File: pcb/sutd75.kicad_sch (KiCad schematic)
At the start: 44 parts, among them J1 SWD Header, J2 Development header, J3 USB_C_Receptacle_USB2.0, J4 Display I2C, SW1 BOOT0, SW2 BOOT1, SW3 RESET, U1 XC6206PxxxMR, U2 STM32F103RBTx, U3 USBLC6-2SC6

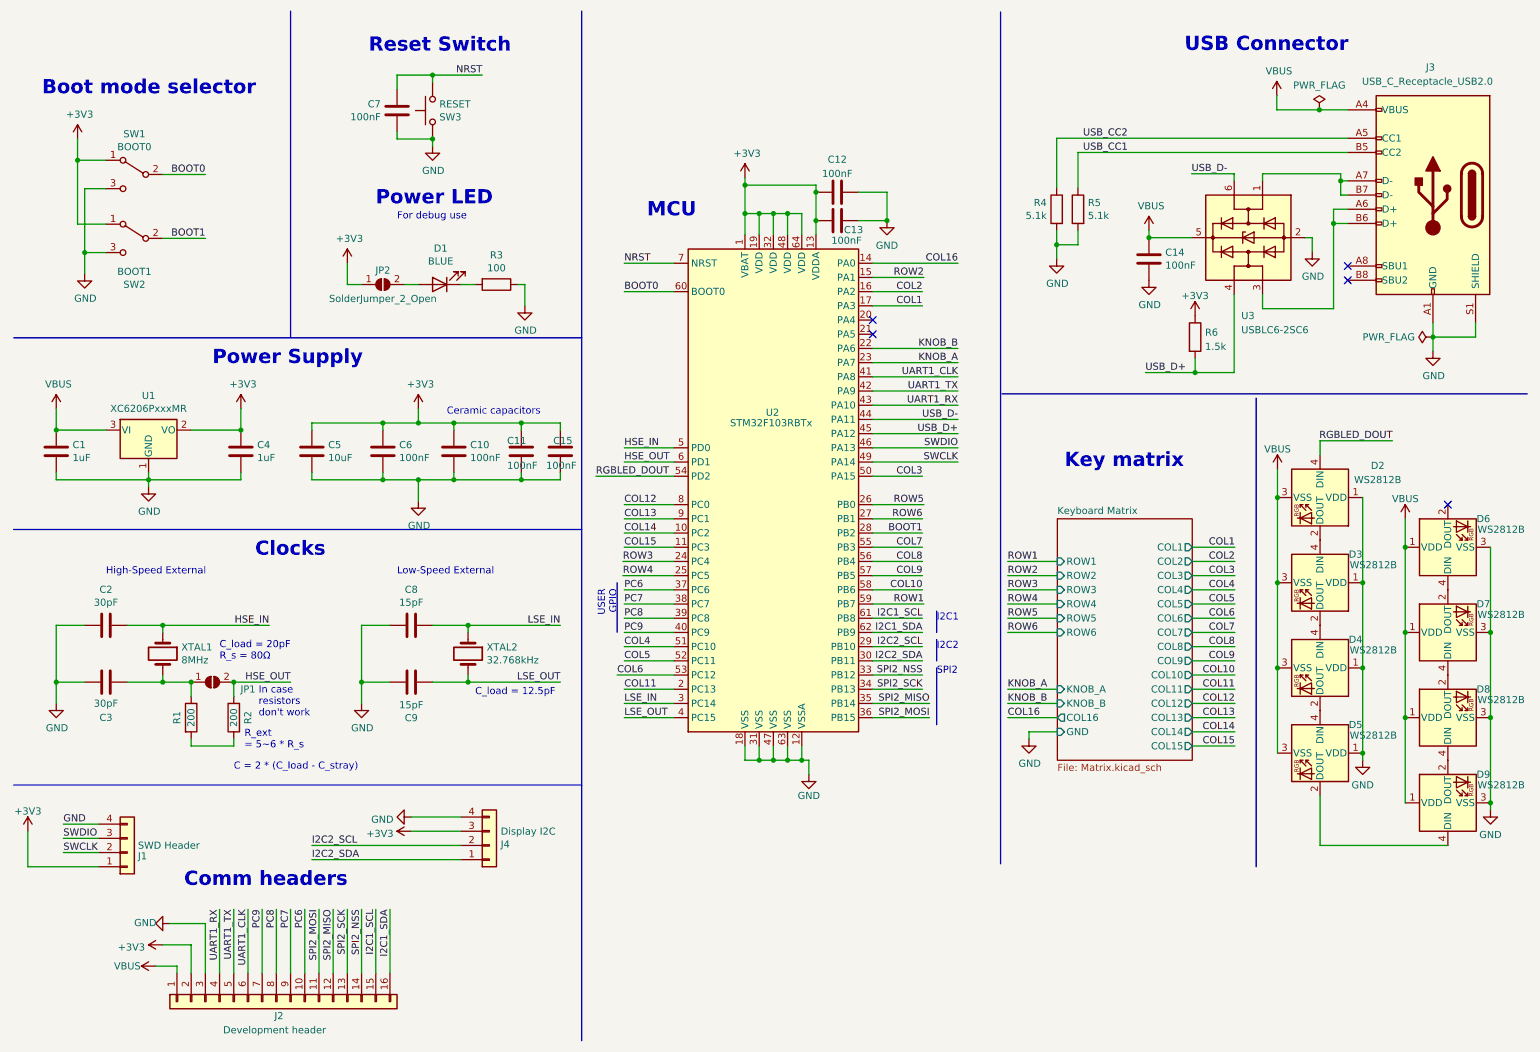
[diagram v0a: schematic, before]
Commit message: Add optional pullup resistors to I2C screen footprint, update footprints
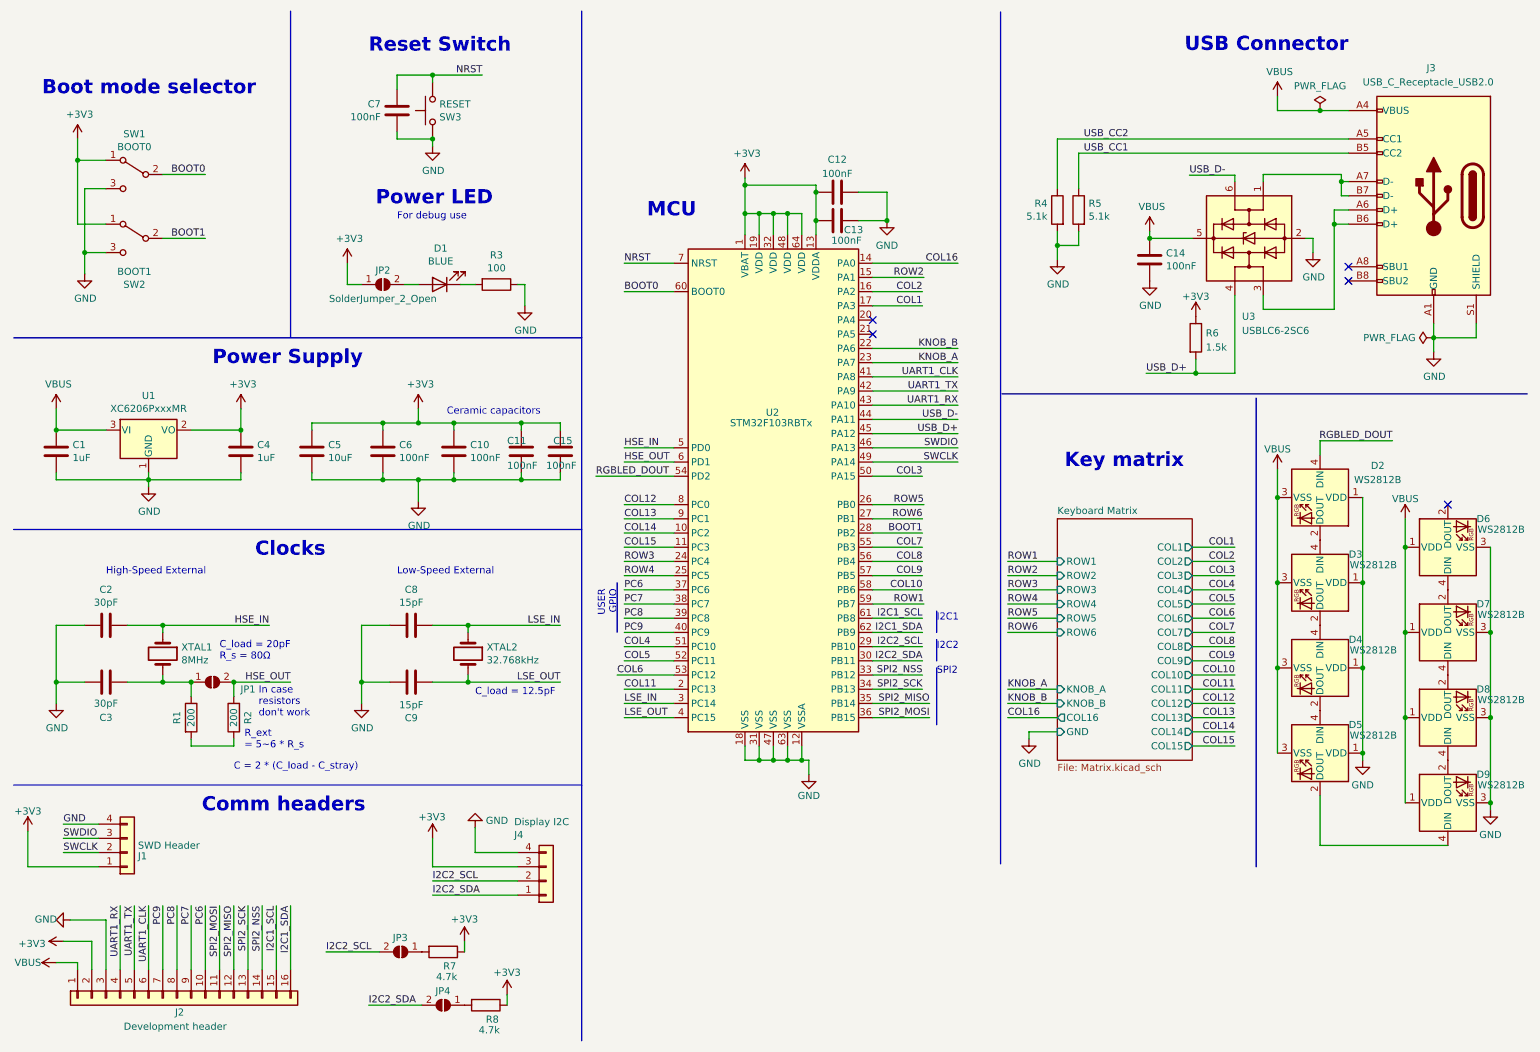
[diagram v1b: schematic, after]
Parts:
- added JP3, JP4: SolderJumper_2_Open, Jumper:SolderJumper-2_P1.3mm_Open_TrianglePad1.0x1.5mm, symbol Jumper:SolderJumper_2_Open
- added R7, R8: 4.7k, Resistor_SMD:R_0402_1005Metric, symbol Device:R
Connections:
- net +3V3: now also R7.1, R8.1
- net I2C2_SCL: now also JP3.2 (B)
- net I2C2_SDA: now also JP4.2 (B)
- new net: JP3.1 (A), R7.2
- new net: JP4.1 (A), R8.2
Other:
- moved on the sheet: J2, J4

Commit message: Touch up silkscreen and schematic
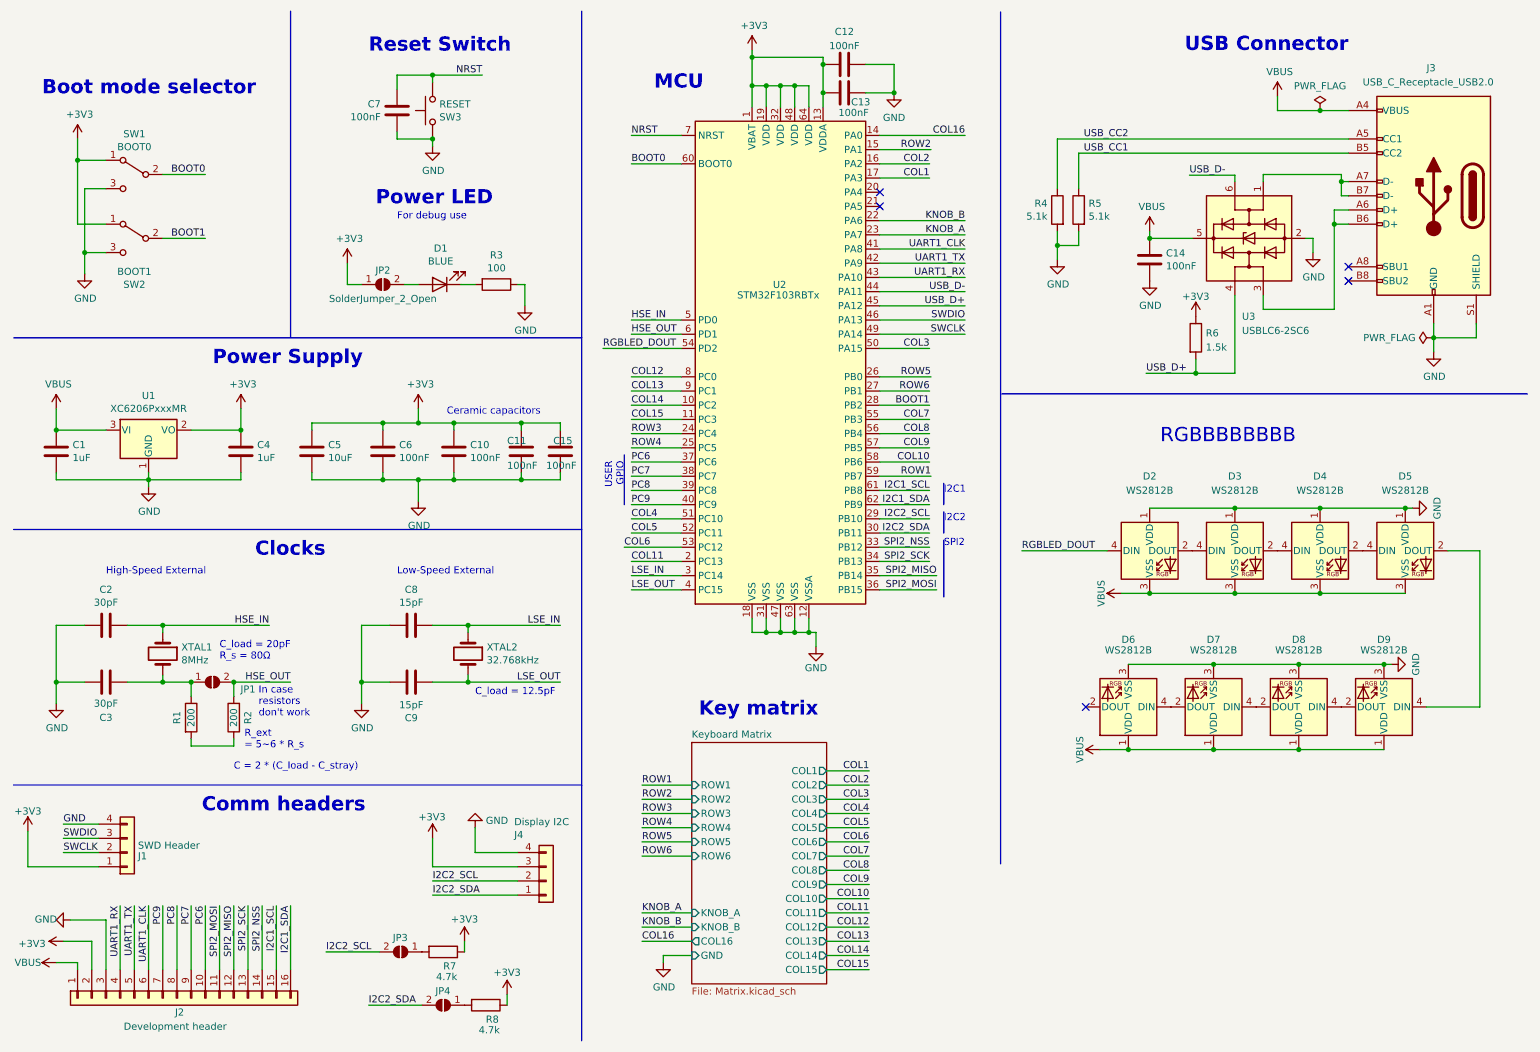
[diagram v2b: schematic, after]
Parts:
- R7, R8: footprint Resistor_SMD:R_0402_1005Metric -> Resistor_SMD:R_0603_1608Metric
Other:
- note added: "RGBBBBBBBB"
- moved on the sheet: C12, C13, D2, D3, D4, D5, D6, D7, D8, D9, U2

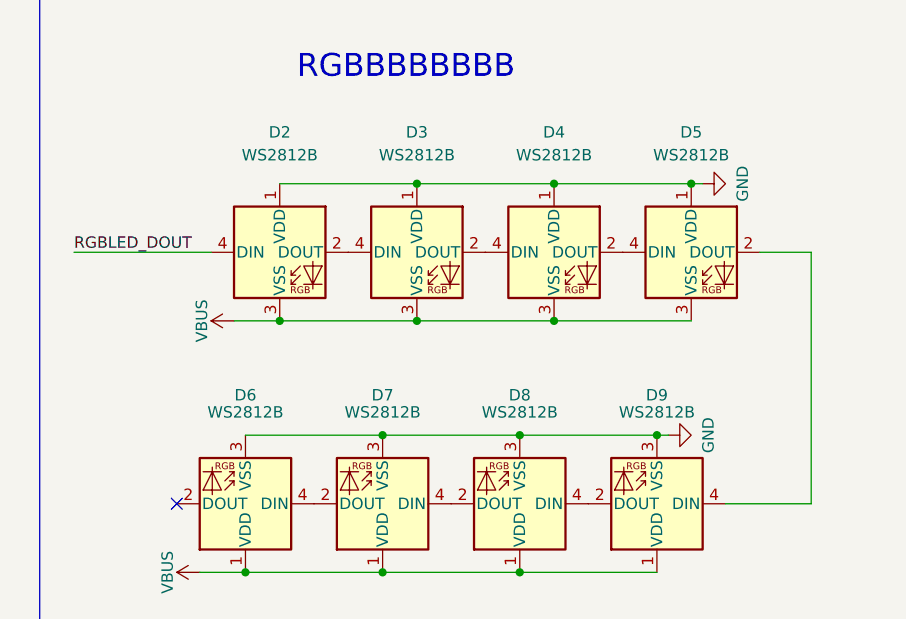
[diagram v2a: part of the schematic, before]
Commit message: Fix SWD silkscreen and boot toggles
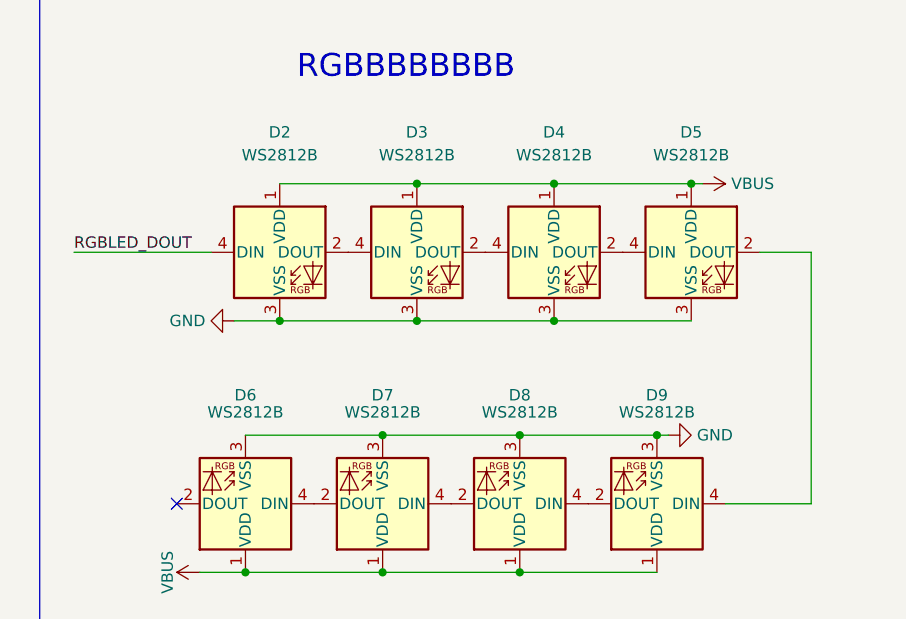
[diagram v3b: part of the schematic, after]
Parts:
- R7, R8: LSCS (none) -> C423031
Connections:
- net GND: now also D2.3 (VSS), D3.3 (VSS), D4.3 (VSS), D5.3 (VSS); no longer D2.1 (VDD), D3.1 (VDD), D4.1 (VDD), D5.1 (VDD)
- net VBUS: now also D2.1 (VDD), D3.1 (VDD), D4.1 (VDD), D5.1 (VDD); no longer D2.3 (VSS), D3.3 (VSS), D4.3 (VSS), D5.3 (VSS)
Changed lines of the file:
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@@
     )
   )
-  (symbol (lib_id "power:GND") (at 264.16 102.235 90) (unit 1)
+  (symbol (lib_id "power:GND") (at 212.09 117.475 270) (unit 1)
     (in_bom yes) (on_board yes) (dnp no) (fields_autoplaced)
-    (property "Reference" "#PWR04" (at 270.51 102.235 0)
-      (effects (font (size 1.27 1.27)) hide)
-    )
-    (property "Value" "GND" (at 268.6034 102.235 0)
-      (effects (font (size 1.27 1.27)))
-    )
-    (property "Footprint" "" (at 264.16 102.235 0)
-      (effects (font (size 1.27 1.27)) hide)
-    )
-    (property "Datasheet" "" (at 264.16 102.235 0)
+    (property "Reference" "#PWR04" (at 205.74 117.475 0)
+      (effects (font (size 1.27 1.27)) hide)
+    )
+    (property "Value" "GND" (at 208.9151 117.475 90)
+      (effects (font (size 1.27 1.27)) (justify right))
+    )
+    (property "Footprint" "" (at 212.09 117.475 0)
+      (effects (font (size 1.27 1.27)) hide)
+    )
+    (property "Datasheet" "" (at 212.09 117.475 0)
       (effects (font (size 1.27 1.27)) hide)
     )
@@
     )
   )
-  (symbol (lib_id "power:VBUS") (at 212.09 117.475 90) (unit 1)
+  (symbol (lib_id "power:VBUS") (at 264.16 102.235 270) (unit 1)
     (in_bom yes) (on_board yes) (dnp no) (fields_autoplaced)
-    (property "Reference" "#PWR03" (at 215.9 117.475 0)
-      (effects (font (size 1.27 1.27)) hide)
-    )
-    (property "Value" "VBUS" (at 208.5142 117.475 0)
-      (effects (font (size 1.27 1.27)))
-    )
-    (property "Footprint" "" (at 212.09 117.475 0)
-      (effects (font (size 1.27 1.27)) hide)
-    )
-    (property "Datasheet" "" (at 212.09 117.475 0)
+    (property "Reference" "#PWR03" (at 260.35 102.235 0)
+      (effects (font (size 1.27 1.27)) hide)
+    )
+    (property "Value" "VBUS" (at 267.335 102.235 90)
+      (effects (font (size 1.27 1.27)) (justify left))
+    )
+    (property "Footprint" "" (at 264.16 102.235 0)
+      (effects (font (size 1.27 1.27)) hide)
+    )
+    (property "Datasheet" "" (at 264.16 102.235 0)
       (effects (font (size 1.27 1.27)) hide)
     )
@@
       (effects (font (size 1.27 1.27)) hide)
     )
-    (property "Value" "GND" (at 264.7934 130.175 0)
-      (effects (font (size 1.27 1.27)))
+    (property "Value" "GND" (at 263.525 130.175 90)
+      (effects (font (size 1.27 1.27)) (justify right))
     )
     (property "Footprint" "" (at 260.35 130.175 0)
@@
       (effects (font (size 1.27 1.27)) hide)
     )
+    (property "LSCS" "C423031" (at 98.425 191.135 90)
+      (effects (font (size 1.27 1.27)) hide)
+    )
     (pin "1")
     (pin "2")
@@
       (effects (font (size 1.27 1.27)) hide)
     )
+    (property "LSCS" "C423031" (at 90.805 181.61 90)
+      (effects (font (size 1.27 1.27)) hide)
+    )

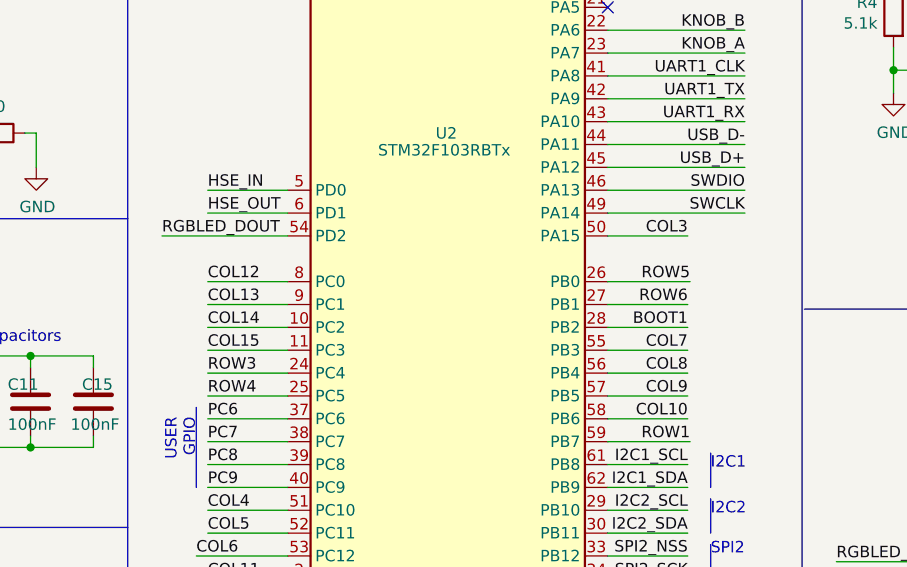
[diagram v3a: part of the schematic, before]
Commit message: Move RGBLED_DIN line to a PWM pin, fix rotary encoder pad overlap
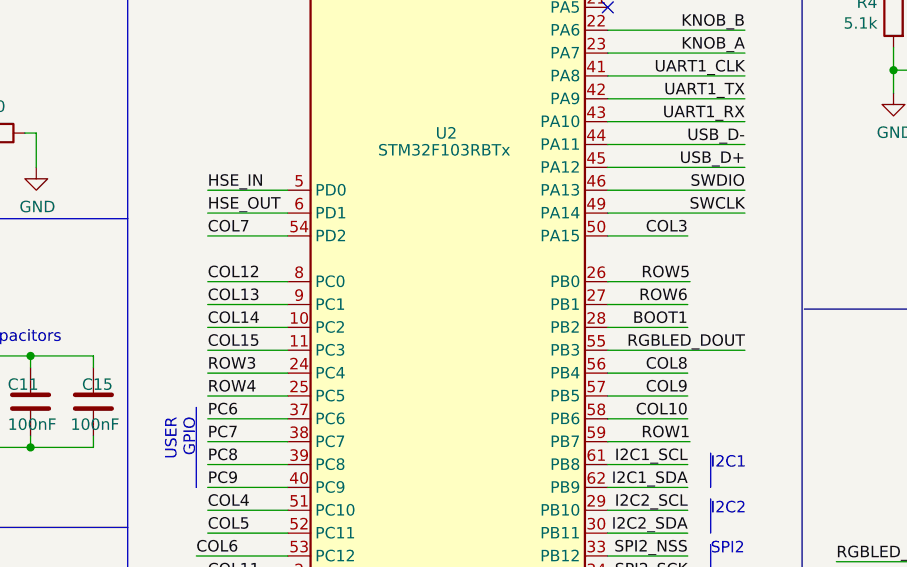
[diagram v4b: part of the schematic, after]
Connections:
- net COL7: now also U2.54 (PD2); no longer U2.55 (PB3)
- net RGBLED_DOUT: now also U2.55 (PB3); no longer U2.54 (PD2)
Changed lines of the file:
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@@
     (stroke (width 0) (type default))
   )
-  (wire (pts (xy 177.8 86.36) (xy 168.91 86.36))
+  (wire (pts (xy 184.15 86.36) (xy 168.91 86.36))
     (stroke (width 0) (type default))
   )
@@
     (stroke (width 0) (type default))
   )
-  (wire (pts (xy 119.38 73.66) (xy 133.35 73.66))
+  (wire (pts (xy 124.46 73.66) (xy 133.35 73.66))
     (stroke (width 0) (type default))
   )
@@
     (effects (font (size 1.27 1.27)) (justify left bottom))
   )
-  (label "COL7" (at 177.8 86.36 180) (fields_autoplaced)
-    (effects (font (size 1.27 1.27)) (justify right bottom))
+  (label "COL7" (at 124.46 73.66 0) (fields_autoplaced)
+    (effects (font (size 1.27 1.27)) (justify left bottom))
   )
   (label "COL10" (at 167.005 172.085 180) (fields_autoplaced)
@@
     (effects (font (size 1.27 1.27)) (justify left bottom))
   )
-  (label "RGBLED_DOUT" (at 119.38 73.66 0) (fields_autoplaced)
-    (effects (font (size 1.27 1.27)) (justify left bottom))
+  (label "RGBLED_DOUT" (at 184.15 86.36 180) (fields_autoplaced)
+    (effects (font (size 1.27 1.27)) (justify right bottom))
   )
   (label "COL1" (at 167.005 149.225 180) (fields_autoplaced)
